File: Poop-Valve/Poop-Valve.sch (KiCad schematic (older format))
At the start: 21 parts

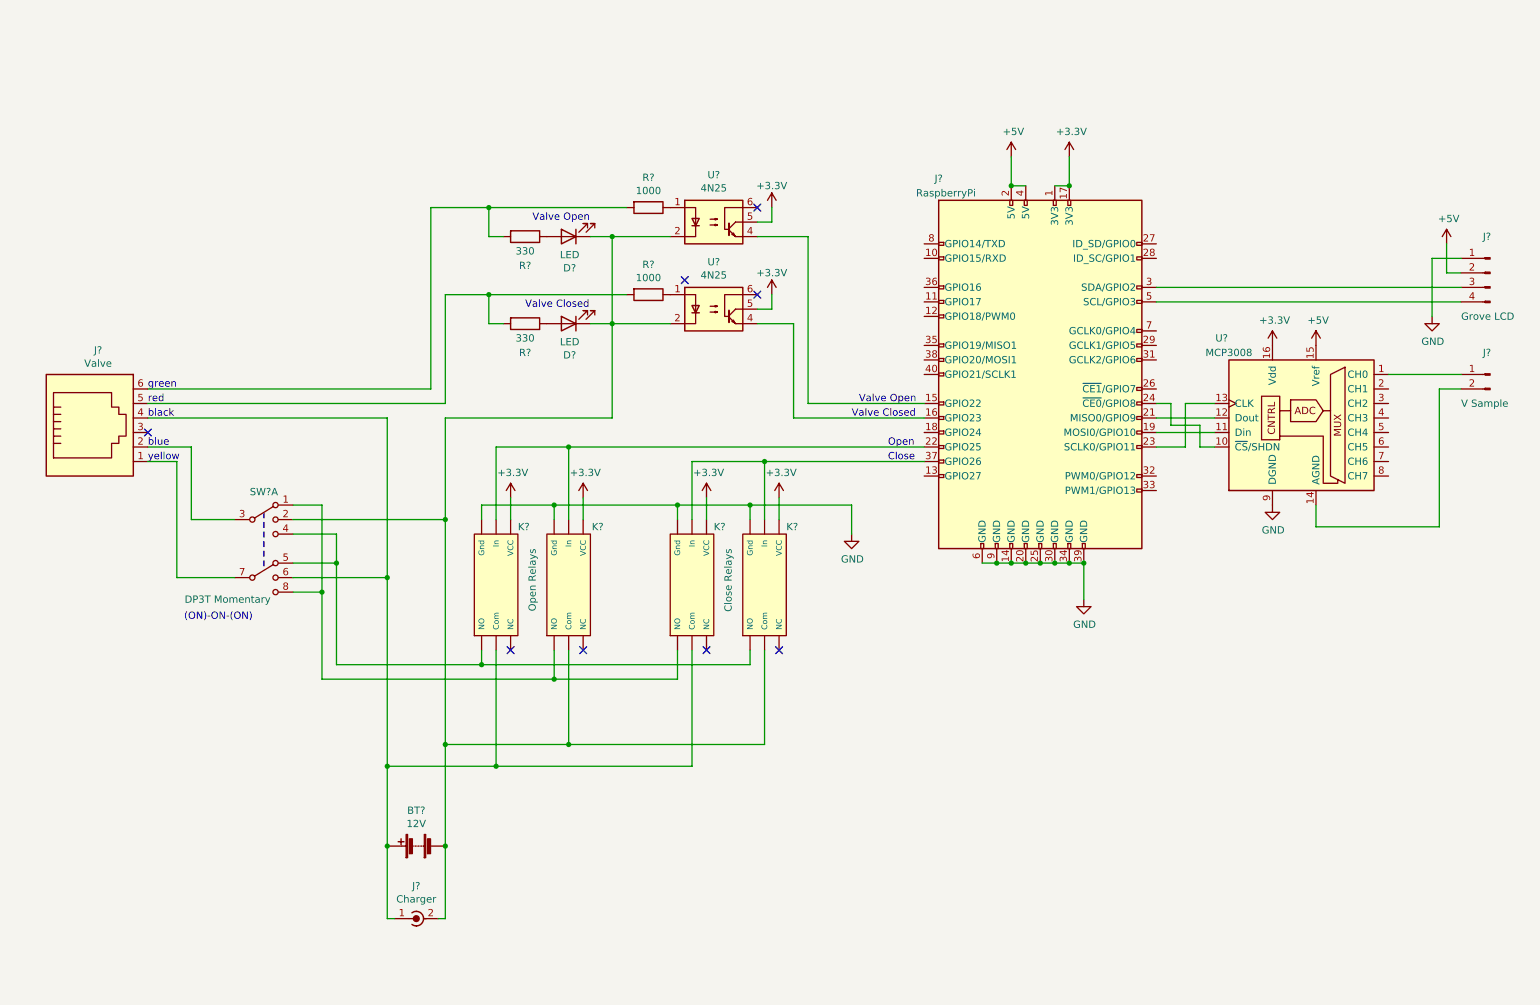
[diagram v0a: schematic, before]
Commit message: v0.2 changed relay configuration
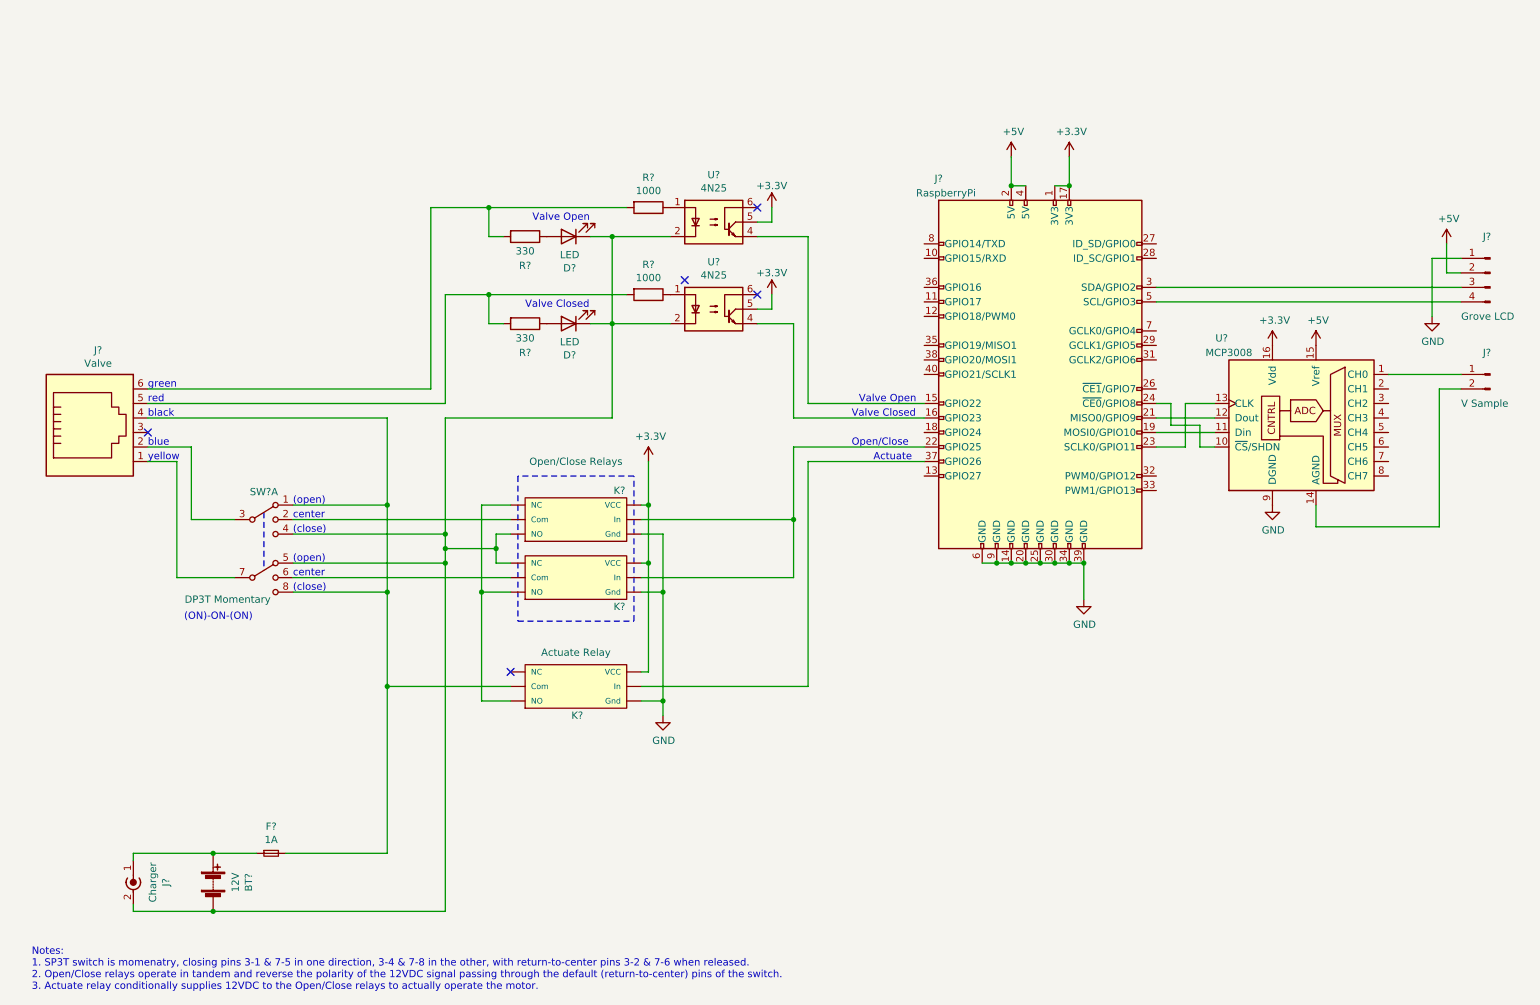
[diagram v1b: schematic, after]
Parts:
- removed K?: Close Relays, symbol myLib:Relay_Module
- removed K?: Open Relays, symbol myLib:Relay_Module
- removed K?: Relay_Module, symbol myLib:Relay_Module
- added F?: 1A, symbol Device:Fuse_Small
- added K?: Open/Close Relays, symbol myLib:Relay_Module
- added K?: Polarity Reverse, symbol myLib:Relay_Module
- K?: value Relay_Module -> Actuate Relay
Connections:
- net +3V3: now also K?.~ (VCC), K?.~ (VCC)
- net GND: now also K?.~ (VCC), K?.~ (VCC)
- net at J?.22 (GPIO25): now also K?.~ (VCC), K?.~ (VCC)
- net at BT?.2 (-), D?.1 (K), D?.1 (K)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: now also SW?.4, SW?.5, K?.~ (VCC), K?.~ (VCC); no longer K?.~ (VCC), SW?.2
- net at BT?.1 (+), J?.1 (In): now also F?.1; no longer J?.4, SW?.6
- net at SW?.1, SW?.8: now also J?.4, K?.~ (VCC), F?.2
- new net: K?.~ (VCC), K?.~ (VCC), K?.~ (VCC)
- new net: K?.~ (VCC), SW?.2
- new net: K?.~ (VCC), SW?.6
- no-connect marks 8 -> 5
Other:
- note added: "(close)"
- note added: "(open)"
- note added: "Actuate"
- note added: "Notes:\n1. SP3T switch is momenatry, closing pins 3-1 & 7-5 in one direction, 3-4 & 7-8 in the other, with return-to-center pins 3-2 & 7-6 when released.\n2. Open/Close relays operate in tandem and reverse the polarity of the 12VDC signal passing through the default (return-to-center) pins of the switch.\n3. Actuate relay conditionally supplies 12VDC to the Open/Close relays to actually operate t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"
- note added: "Open/Close"
- note added: "center"
- note removed: "Close"
- note removed: "Open"
- moved on the sheet: BT?, J?, K?

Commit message: v0.3 pivot to maual override relay
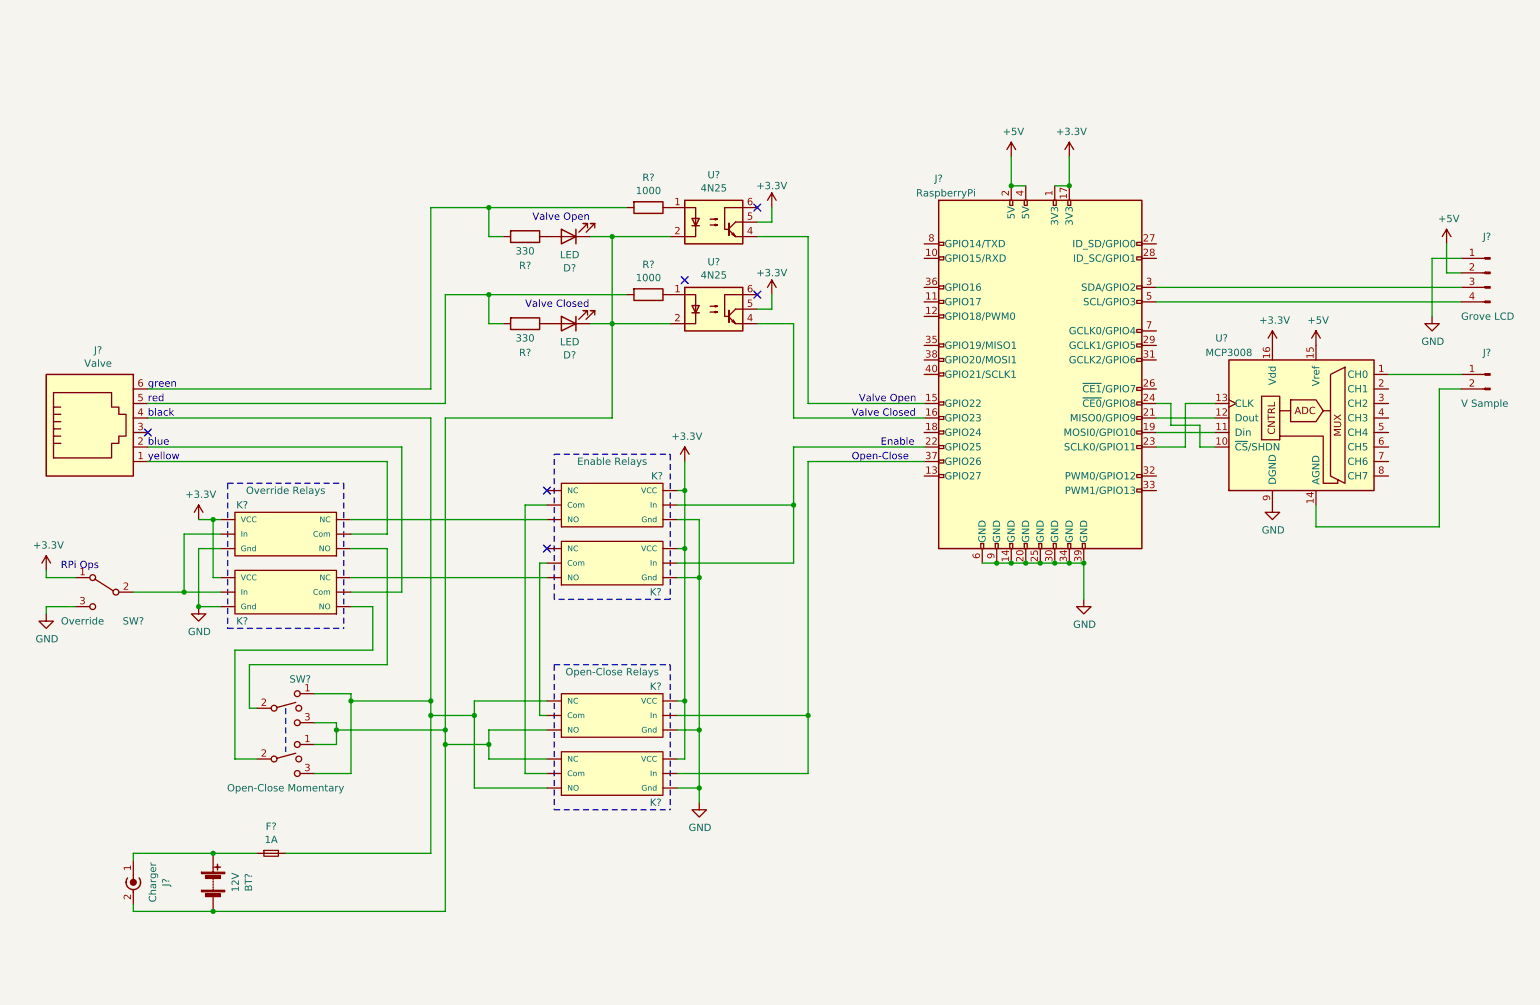
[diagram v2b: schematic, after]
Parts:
- removed K?: Open/Close Relays, symbol myLib:Relay_Module
- removed K?: Polarity Reverse, symbol myLib:Relay_Module
- removed SW?: SW_DP3T, symbol Switch:SW_DP3T
- removed SW?: DP3T Momentary, symbol Switch:SW_DP3T
- added K?: Relay_Module, symbol myLib:Relay_Module
- added K?: Override Relays, symbol myLib:Relay_Module
- added K? (x2): Polarity Reverse, symbol myLib:Relay_Module
- added K?: Open-Close Relays, symbol myLib:Relay_Module
- added SW?: Open-Close Momentary, symbol Switch:SW_SPDT_MSM
- added SW?: SW_SPDT_MSM, symbol Switch:SW_SPDT_MSM
- added SW?: Override, symbol Switch:SW_SPDT
- K?: value Actuate Relay -> Enable Relays
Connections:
- net +3V3: now also K?.~ (VCC), K?.~ (VCC), K?.~ (VCC), K?.~ (VCC), K?.~ (VCC), SW?.1 (A)
- net GND: now also K?.~ (VCC), K?.~ (VCC), K?.~ (VCC), K?.~ (VCC), K?.~ (VCC), SW?.3 (C)
- net at J?.22 (GPIO25): now also K?.~ (VCC), K?.~ (VCC)
- net at J?.37 (GPIO26): now also K?.~ (VCC), K?.~ (VCC); no longer K?.~ (VCC)
- net at BT?.2 (-), D?.1 (K), D?.1 (K)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: now also K?.~ (VCC), K?.~ (VCC), SW?.1, SW?.3
- net at F?.2, J?.4: now also K?.~ (VCC), K?.~ (VCC), SW?.1, SW?.3; no longer K?.~ (VCC)
- net at J?.1: now also K?.~ (VCC)
- net at J?.2: now also K?.~ (VCC)
- new net: K?.~ (VCC), K?.~ (VCC) (x4)
- new net: K?.~ (VCC), K?.~ (VCC), SW?.2 (B)
- new net: K?.~ (VCC), SW?.2 (x2)
- no-connect marks 5 -> 6
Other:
- note added: "Enable"
- note added: "Open-Close"
- note added: "RPi Ops"
- note removed: "(ON)-ON-(ON)"
- note removed: "(close)"
- note removed: "(open)"
- note removed: "Actuate"
- note removed: "Notes:\n1. SP3T switch is momenatry, closing pins 3-1 & 7-5 in one direction, 3-4 & 7-8 in the other, with return-to-center pins 3-2 & 7-6 when released.\n2. Open/Close relays operate in tandem and reverse the polarity of the 12VDC signal passing through the default (return-to-center) pins of the switch.\n3. Actuate relay conditionally supplies 12VDC to the Open/Close relays to actually operate t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"
- note removed: "Open/Close"
- note removed: "center"
- moved on the sheet: K?

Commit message: cleaned up some lables
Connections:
- new net: J?.22 (GPIO25), K?.~ (VCC), K?.~ (VCC)
- new net: J?.37 (GPIO26), K?.~ (VCC), K?.~ (VCC)
- new net: K?.~ (VCC), K?.~ (VCC) (x4)
- new net: K?.~ (VCC), K?.~ (VCC), SW?.2 (B)
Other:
- note added: "* GPIO26 logic:\n Open is high\n Close is low"
- note added: "* Open-Close"
- note added: "Center"
- note added: "Close"
- note added: "Open"
- note added: "Sense Valve Closed\n"
- note added: "Sense Valve Open"
- note removed: "Open-Close"
- note removed: "Valve Closed\n"
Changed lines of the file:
@@
 Text Notes 4100 2650 0    50   ~ 0
 Valve Closed
-Text Notes 6400 3300 0    50   ~ 0
-Valve Open
-Text Notes 6350 3400 0    50   ~ 0
-Valve Closed\n
+Text Notes 6150 3300 0    50   ~ 0
+Sense Valve Open
+Text Notes 6100 3400 0    50   ~ 0
+Sense Valve Closed\n
 Text Notes 6550 3600 0    50   ~ 0
 Enable
@@
 	1950 6800 3550 6800
 Connection ~ 1950 6800
-Text Notes 6350 3700 0    50   ~ 0
-Open-Close
+Text Notes 6300 3700 0    50   ~ 0
+* Open-Close
 $Comp
 L power:GND #PWR?
@@
 	1    0    0    -1
 $EndComp
-Wire Wire Line
-	2650 5500 2800 5500
-Wire Wire Line
-	2800 5650 2650 5650
-Wire Wire Line
-	2650 5300 2900 5300
-Wire Wire Line
-	2900 5850 2650 5850
-Wire Wire Line
-	2800 5500 2800 5550
-Wire Wire Line
-	2800 5550 3550 5550
-Connection ~ 2800 5550
-Wire Wire Line
-	2800 5550 2800 5650
 Connection ~ 3550 5550
 Wire Wire Line
@@
 Wire Wire Line
 	3050 4700 2900 4700
-Wire Wire Line
-	2900 5300 2900 5350
-Wire Wire Line
-	2900 5350 3450 5350
-Connection ~ 2900 5350
 Connection ~ 3450 5350
 Wire Wire Line
@@
 Connection ~ 5300 4500
 Wire Wire Line
-	2900 5350 2900 5850
-Wire Wire Line
 	5300 4100 5300 4500
 Wire Wire Line
@@
 Wire Wire Line
 	3850 5650 3850 5750
+Text Notes 2650 5300 0    50   ~ 0
+Open
+Text Notes 2650 5500 0    50   ~ 0
+Close
+Text Notes 2650 5400 0    50   ~ 0
+Center
+Wire Wire Line
+	2950 5300 2950 5350
+Connection ~ 2950 5350
+Wire Wire Line
+	2950 5350 3450 5350
+Wire Wire Line
+	2950 5350 2950 5850
+Wire Wire Line
+	2850 5650 2850 5550
+Connection ~ 2850 5550
+Wire Wire Line
+	2850 5550 3550 5550
+Wire Wire Line
+	2850 5550 2850 5500
+Wire Wire Line
+	2650 5500 2850 5500
+Wire Wire Line
+	2650 5650 2850 5650
+Wire Wire Line
+	2650 5300 2950 5300
+Wire Wire Line
+	2650 5850 2950 5850
+Text Notes 6200 4100 0    50   ~ 0
+* GPIO26 logic:\n  Open is high\n  Close is low
 $EndSCHEMATC

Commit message: v0.4 fix override logic; detect override; resize A4->US
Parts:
- added D?: LED, symbol Device:LED
- added R?: 1000, symbol Device:R
- added R?: 330, symbol Device:R
- added SW?: Manual Override, symbol Switch:SW_SPDT
- added U?: 4N25, Package_DIP:DIP-6_W7.62mm, symbol Isolator:4N25
- K? (x6): symbol myLib:Relay_Module -> Poop-Valve-rescue:Relay_Module-myLib
- SW?: value Open-Close Momentary -> SW_DPDT_x2
- SW?: value SW_SPDT_MSM -> SW_DPDT_x2
- SW?: value Override -> SW_DPDT_x2
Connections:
- net +3V3: now also SW?.3 (C), U?.15 (Vref), SW?.1 (A), U?.5; no longer SW?.1 (A)
- net +5V: no longer U?.15 (Vref)
- net GND: now also SW?.1 (A), D?.1 (K), SW?.3 (C), U?.2; no longer SW?.3 (C)
- net at J?.18 (GPIO24): now also U?.4
- new net: J?.22 (GPIO25), K?.~ (VCC), K?.~ (VCC)
- new net: J?.37 (GPIO26), K?.~ (VCC), K?.~ (VCC)
- new net: K?.~ (VCC), K?.~ (VCC) (x3)
- new net: R?.1, U?.1
- new net: R?.2, R?.2, SW?.2 (B)
- new net: K?.~ (VCC), K?.~ (VCC), SW?.2 (B)
- new net: D?.2 (A), R?.1
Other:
- note added: "Override"
- note added: "RPi"
- note added: "Sense Override (invert)"
- note removed: "RPi Ops"
- moved on the sheet: D?, J?, K?, R?, SW?, U?
